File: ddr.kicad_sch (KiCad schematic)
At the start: 29 parts, among them U1 MIMX8MM6DVTLZAA, U3 MT40A1G16KD-062E

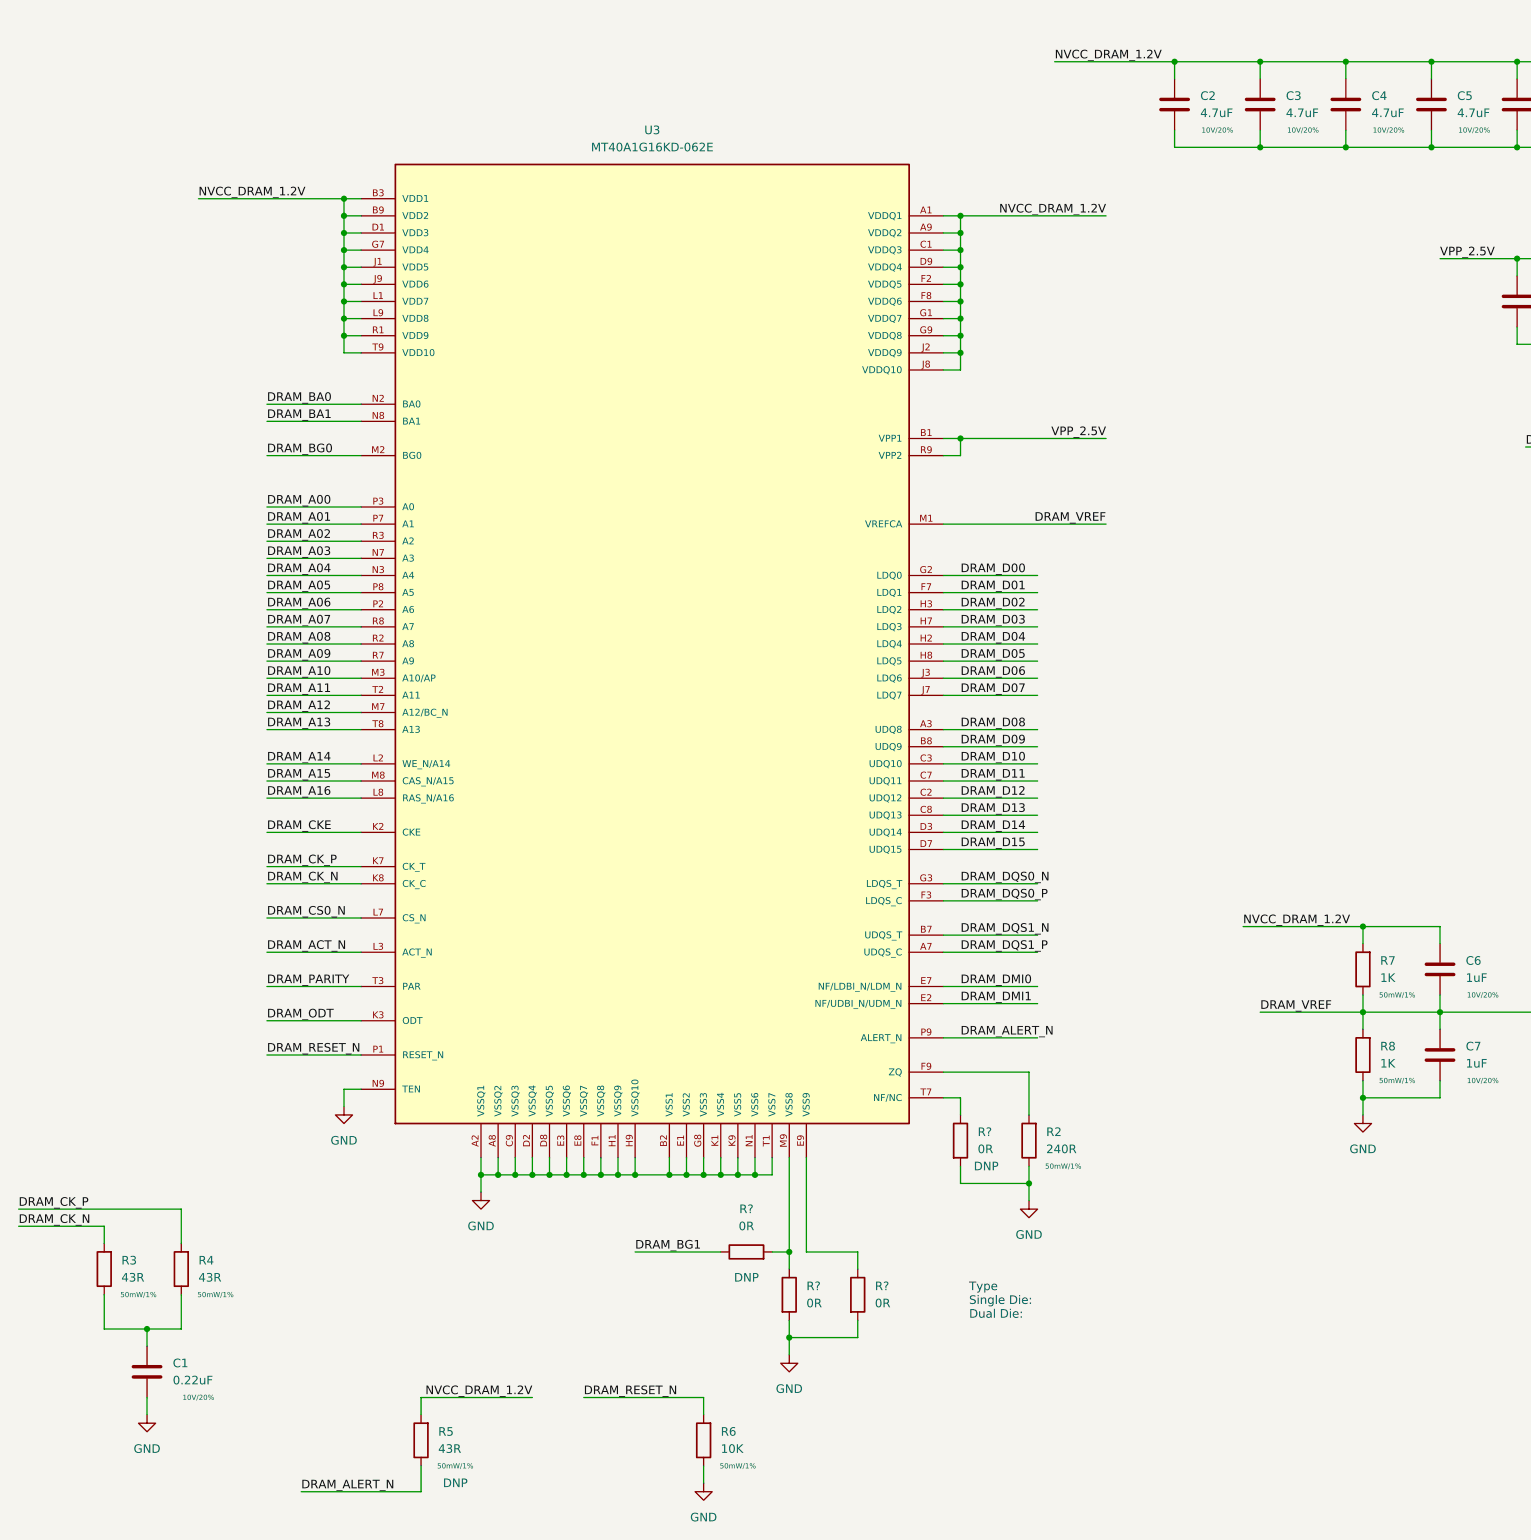
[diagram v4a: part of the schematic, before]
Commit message: fix ref desgigators, add table for dram config
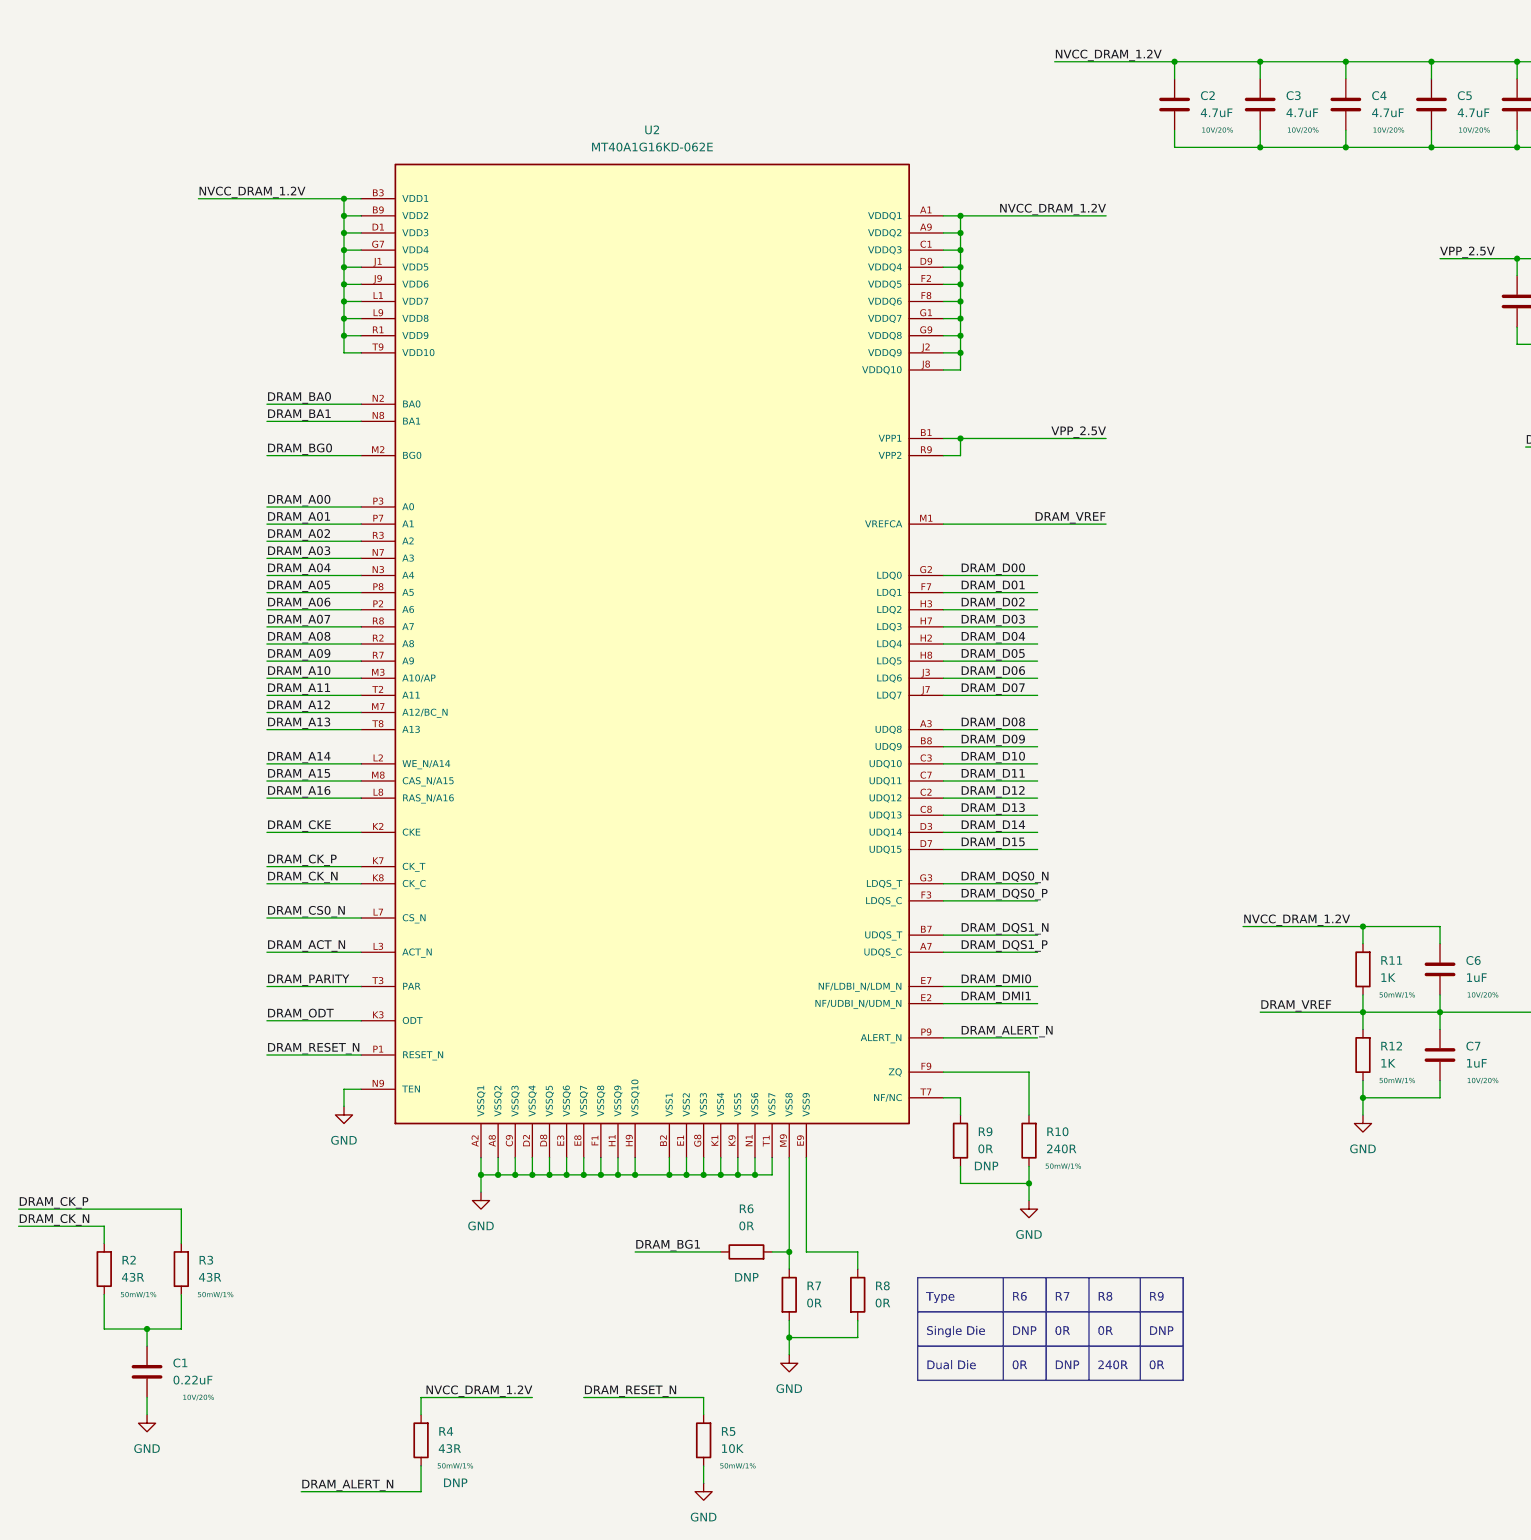
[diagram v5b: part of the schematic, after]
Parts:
- gave numbers to parts that had none: 4
- renumbered R2 to R10, R7 to R11, R8 to R12, R3 to R2, R4 to R3, R5 to R4, R6 to R5, U3 to U2
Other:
- note added: "0R"
- note added: "240R"
- note added: "DNP"
- note added: "Dual Die"
- note added: "R6"
- note added: "R7"
- note added: "R8"
- note added: "R9"
- note added: "Single Die"
- note added: "Type"
- note removed: "Type Single Die: Dual Die:"

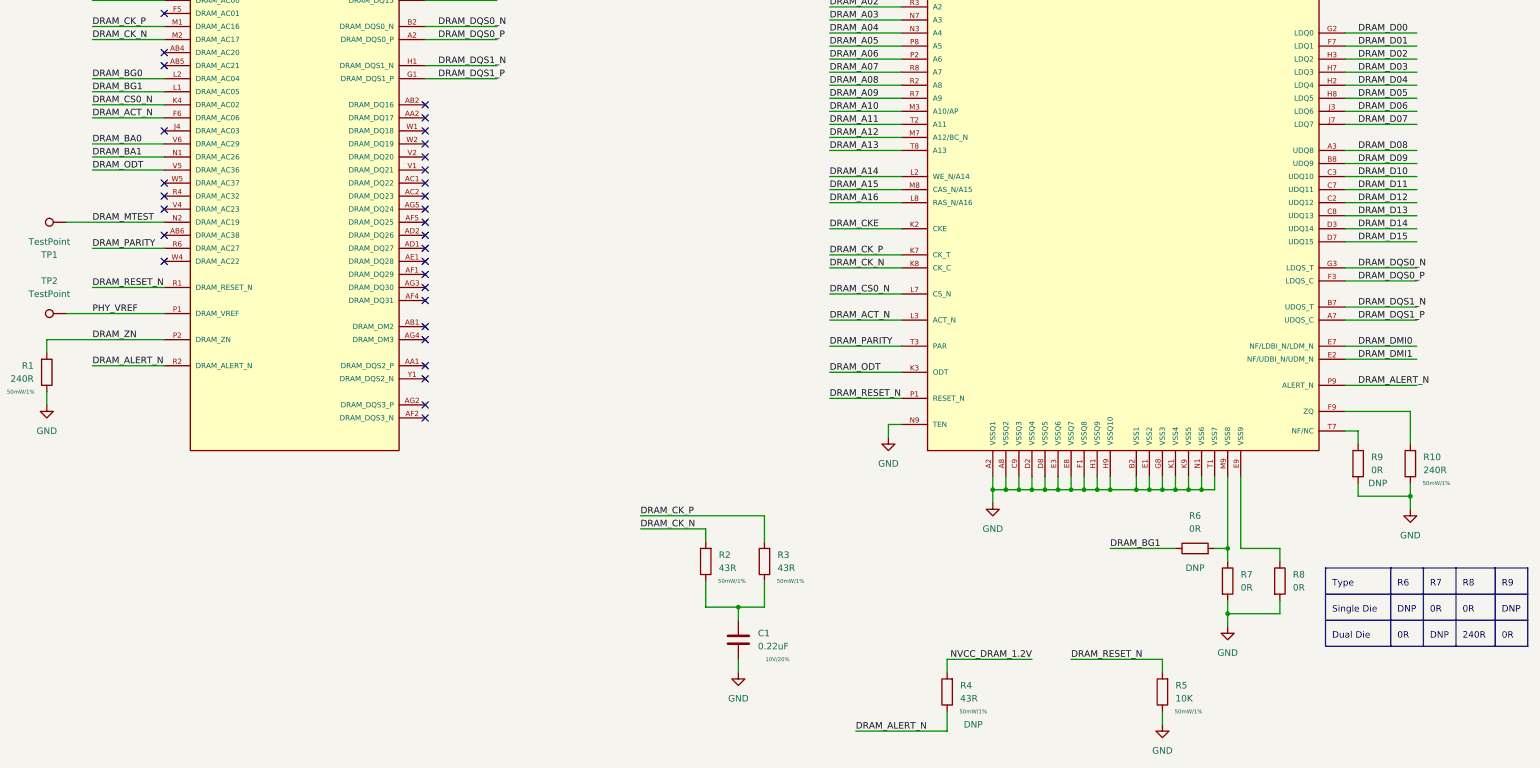
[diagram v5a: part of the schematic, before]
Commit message: add ddr vpp ldo, fix ddr net names
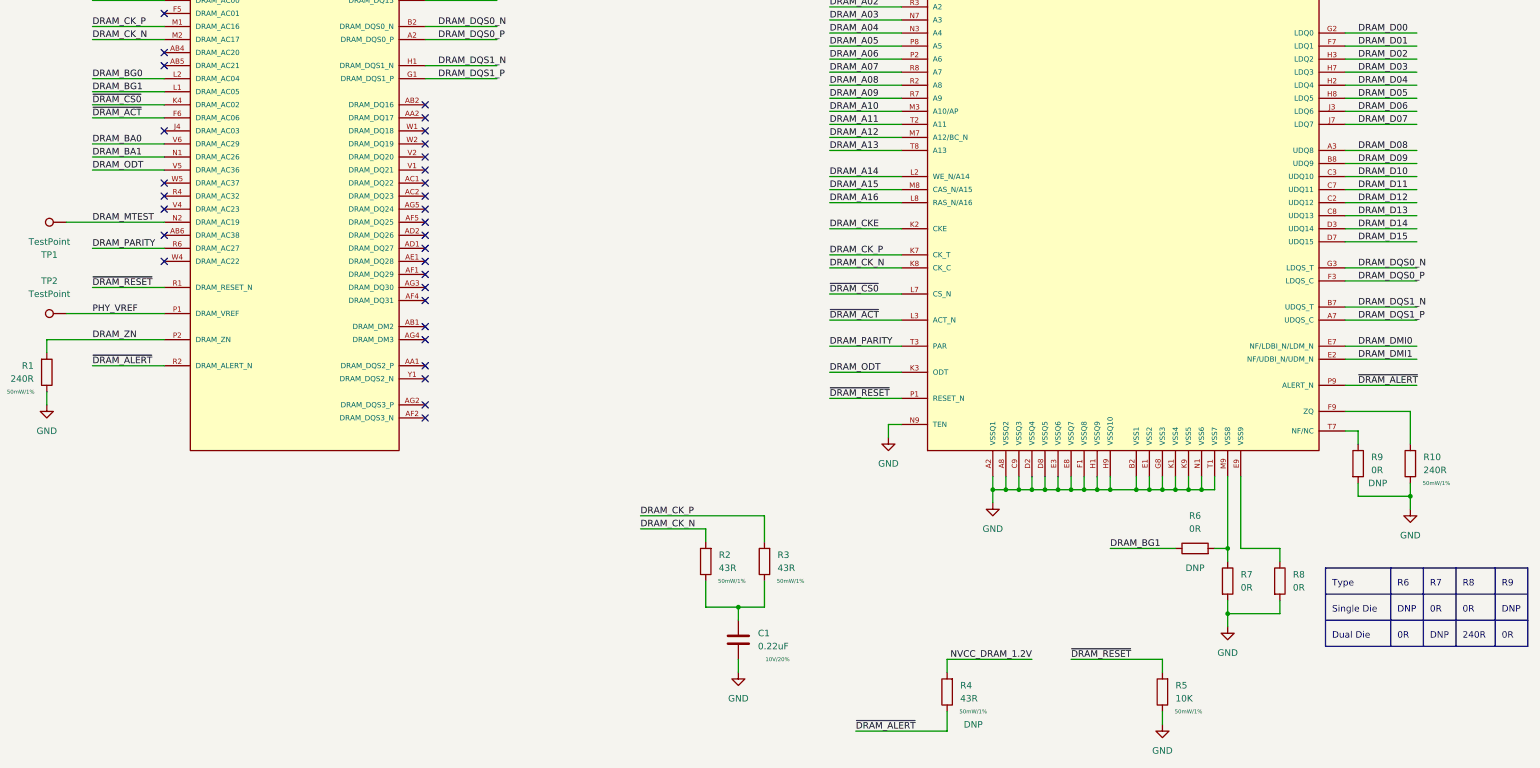
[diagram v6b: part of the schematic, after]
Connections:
- net DRAM_ACT_N renamed ~{DRAM_ACT}
- net DRAM_ALERT_N renamed ~{DRAM_ALERT}
- net DRAM_CS0_N renamed ~{DRAM_CS0}
- net DRAM_RESET_N renamed ~{DRAM_RESET}
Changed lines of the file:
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@@
     (effects (font (size 1.27 1.27)) (justify left bottom))
   )
-  (label "DRAM_RESET_N" (at 194.31 180.34 0)
+  (label "~{DRAM_RESET}" (at 194.31 180.34 0)
     (effects (font (size 1.27 1.27)) (justify left bottom))
   )
@@
   )
   (label "DRAM_D11" (at 118.11 92.71 0)
-    (effects (font (size 1.27 1.27)) (justify left bottom))
-  )
-  (label "DRAM_ALERT_N" (at 297.18 177.8 0)
     (effects (font (size 1.27 1.27)) (justify left bottom))
   )
@@
     (effects (font (size 1.27 1.27)) (justify left bottom))
   )
-  (label "DRAM_ACT_N" (at 50.8 125.73 0)
+  (label "~{DRAM_ACT}" (at 50.8 125.73 0)
     (effects (font (size 1.27 1.27)) (justify left bottom))
   )
@@
     (effects (font (size 1.27 1.27)) (justify left bottom))
   )
+  (label "~{DRAM_ALERT}" (at 297.18 177.8 0)
+    (effects (font (size 1.27 1.27)) (justify left bottom))
+  )
   (label "NVCC_DRAM_1.2V" (at 43.18 24.13 0)
     (effects (font (size 1.27 1.27)) (justify left bottom))
@@
     (effects (font (size 1.27 1.27)) (justify left bottom))
   )
+  (label "~{DRAM_RESET}" (at 50.8 158.75 0)
+    (effects (font (size 1.27 1.27)) (justify left bottom))
+  )
   (label "DRAM_ODT" (at 194.31 175.26 0)
     (effects (font (size 1.27 1.27)) (justify left bottom))
@@
     (effects (font (size 1.27 1.27)) (justify left bottom))
   )
-  (label "DRAM_ALERT_N" (at 50.8 173.99 0)
+  (label "~{DRAM_ALERT}" (at 50.8 173.99 0)
     (effects (font (size 1.27 1.27)) (justify left bottom))
   )
@@
     (effects (font (size 1.27 1.27)) (justify left bottom))
   )
+  (label "~{DRAM_ACT}" (at 194.31 165.1 0)
+    (effects (font (size 1.27 1.27)) (justify left bottom))
+  )
   (label "DRAM_A02" (at 194.31 104.14 0)
     (effects (font (size 1.27 1.27)) (justify left bottom))
@@
     (effects (font (size 1.27 1.27)) (justify left bottom))
   )
-  (label "DRAM_ACT_N" (at 194.31 165.1 0)
-    (effects (font (size 1.27 1.27)) (justify left bottom))
-  )
   (label "DRAM_BA1" (at 194.31 86.36 0)
     (effects (font (size 1.27 1.27)) (justify left bottom))
@@
     (effects (font (size 1.27 1.27)) (justify left bottom))
   )
-  (label "DRAM_ALERT_N" (at 199.39 245.11 0)
+  (label "~{DRAM_ALERT}" (at 199.39 245.11 0)
     (effects (font (size 1.27 1.27)) (justify left bottom))
   )
@@
     (effects (font (size 1.27 1.27)) (justify left bottom))
   )
-  (label "DRAM_RESET_N" (at 241.3 231.14 0)
+  (label "~{DRAM_RESET}" (at 241.3 231.14 0)
     (effects (font (size 1.27 1.27)) (justify left bottom))
   )
@@
     (effects (font (size 1.27 1.27)) (justify right bottom))
   )
+  (label "~{DRAM_CS0}" (at 194.31 160.02 0)
+    (effects (font (size 1.27 1.27)) (justify left bottom))
+  )
   (label "DRAM_DQS1_P" (at 118.11 118.11 0)
     (effects (font (size 1.27 1.27)) (justify left bottom))
@@
     (effects (font (size 1.27 1.27)) (justify left bottom))
   )
-  (label "DRAM_CS0_N" (at 50.8 123.19 0)
+  (label "~{DRAM_CS0}" (at 50.8 123.19 0)
     (effects (font (size 1.27 1.27)) (justify left bottom))
   )
@@
     (effects (font (size 1.27 1.27)) (justify left bottom))
   )
-  (label "DRAM_CS0_N" (at 194.31 160.02 0)
-    (effects (font (size 1.27 1.27)) (justify left bottom))
-  )
   (label "DRAM_A08" (at 194.31 119.38 0)
     (effects (font (size 1.27 1.27)) (justify left bottom))
@@
     (effects (font (size 1.27 1.27)) (justify left bottom))
   )
-  (label "DRAM_RESET_N" (at 50.8 158.75 0)
-    (effects (font (size 1.27 1.27)) (justify left bottom))
-  )
